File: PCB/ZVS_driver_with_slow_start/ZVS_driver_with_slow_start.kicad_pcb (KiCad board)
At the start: 2 copper layers, 31 parts, among them J1 Battery_12v_Connection, J2 Power_Switch, J3 ON_switch, J4 Conn_01x02_Socket, Q1 IRF640NPbF, Q2 IRF640NPbF, Q3 IRF640NPbF, U1 OP07, U2 OP07

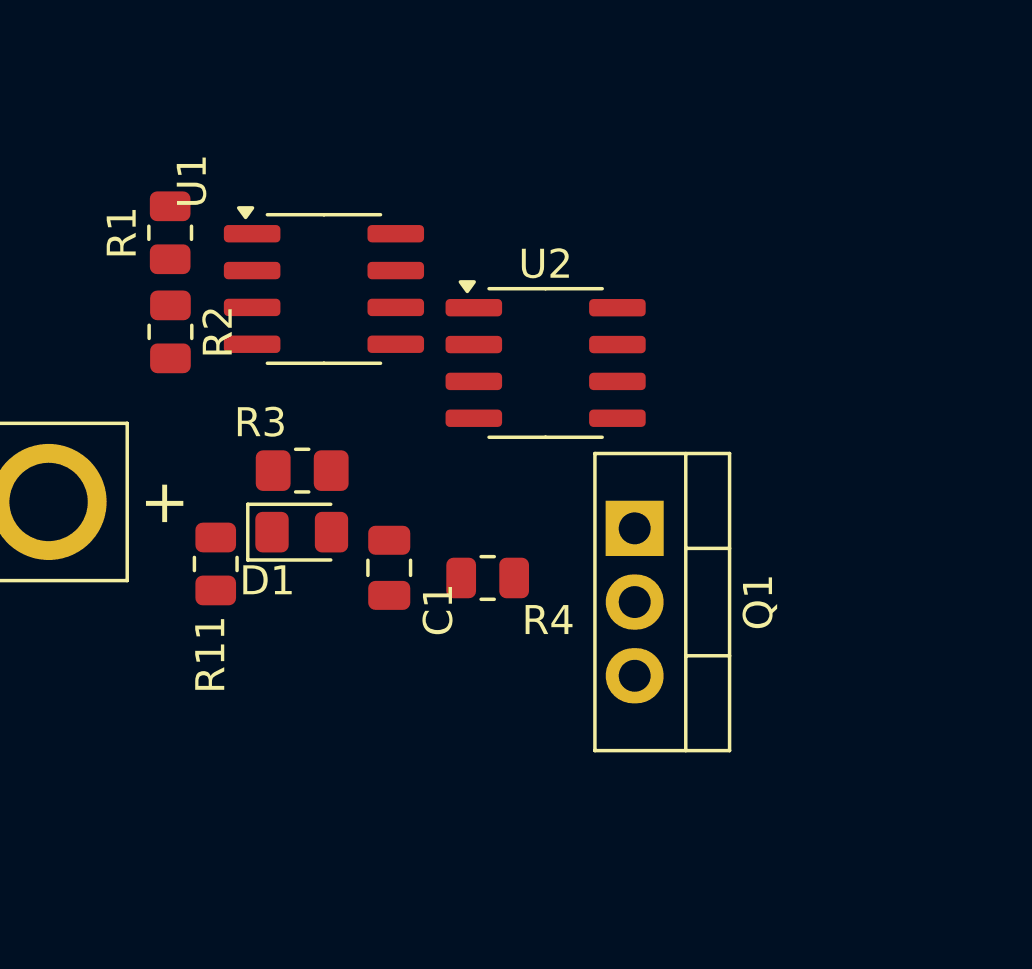
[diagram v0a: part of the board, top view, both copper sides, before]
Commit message: added curent limiting RL on Q1
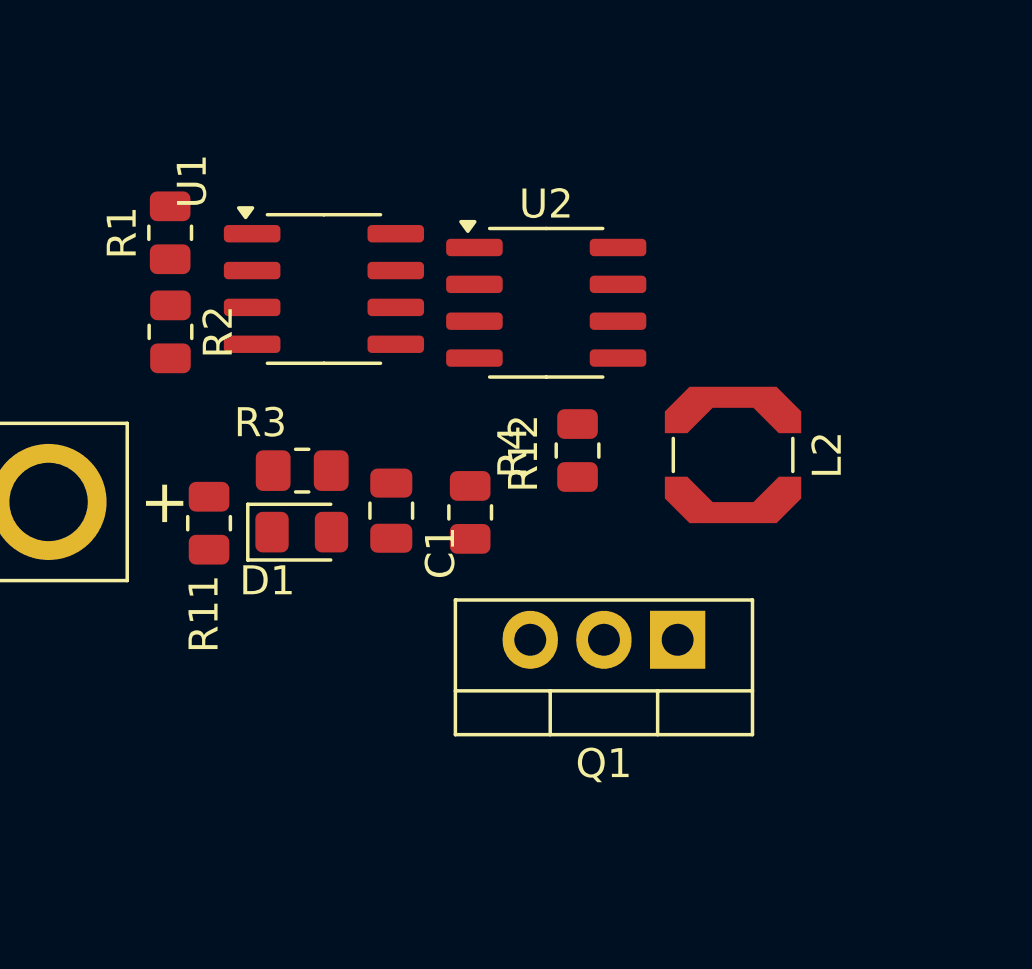
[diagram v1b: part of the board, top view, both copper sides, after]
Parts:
- added L2: 100u, Inductor_SMD:L_Coilcraft_LPS4414, F.Cu at (71.8, 106.5)
- added R12: 100, Resistor_SMD:R_0805_2012Metric, F.Cu at (66.4, 106.4)
- moved Q1 4.12 mm to (69.9, 112.9), turned to 180 degrees
- moved R4 2.34 mm to (62.7, 108.5), turned to -90 degrees
- moved U2 2.08 mm to (65.3, 101.3)
- moved C1 1.97 mm to (60.0, 108.4)
- moved R11 1.42 mm to (53.7, 108.9)
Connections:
- U2 pad 6: Net-(Q1-G) -> Net-(L2-Pad1)

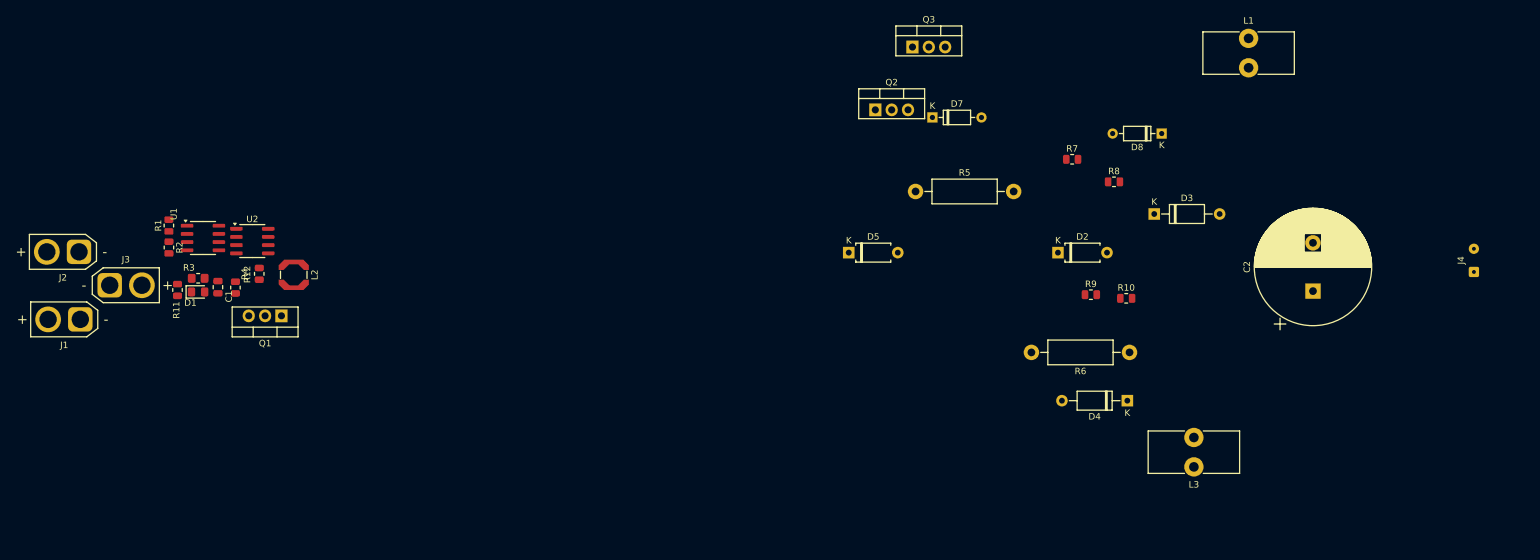
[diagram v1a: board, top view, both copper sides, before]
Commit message: added fuse and cleaned up board
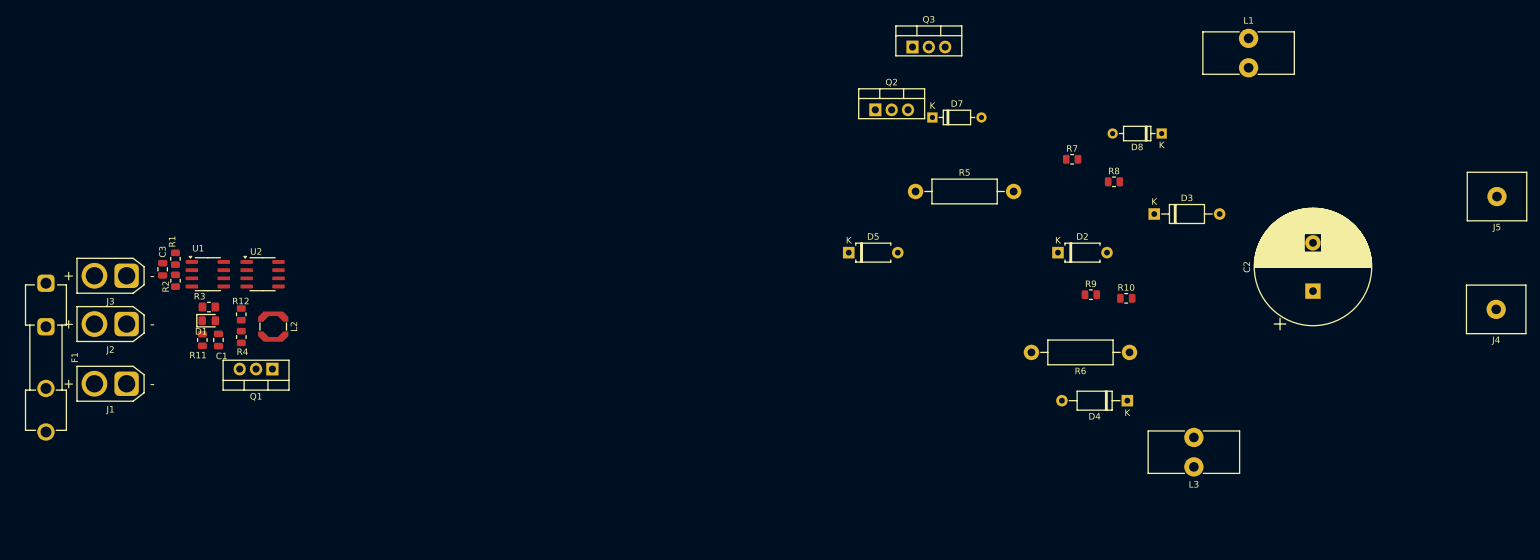
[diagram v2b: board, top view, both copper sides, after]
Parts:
- added C3: 100u, Capacitor_SMD:C_0805_2012Metric, F.Cu at (51.4, 105.7)
- added F1: Fuse, Fuse:Fuseholder_Clip-5x20mm_Keystone_3517_Inline_P23.11x6.76mm_D1.70mm_Horizontal, F.Cu at (33.3, 107.8)
- added J5: Conn_01x01, TerminalBlock_MetzConnect:TerminalBlock_MetzConnect_360271_1x01_Horizontal_ScrewM3.0_Boxed, F.Cu at (258.7, 94.4)
- J4: value Conn_01x02_Socket -> Conn_01x01; footprint Connector_Wire:SolderWire-0.1sqmm_1x02_P3.6mm_D0.4mm_OD1mm -> TerminalBlock_MetzConnect:TerminalBlock_MetzConnect_360271_1x01_Horizontal_ScrewM3.0_Boxed
- moved J2 13.4 mm to (45.8, 114.2)
- moved J1 12.3 mm to (45.8, 123.4)
- moved R11 8.68 mm to (57.6, 116.6)
- moved L2 8.64 mm to (68.6, 114.6)
- moved Q1 8.39 mm to (68.5, 121.2)
- moved C1 8.21 mm to (60.1, 116.6)
- moved R4 7.74 mm to (63.6, 116.2)
- moved R12 6.88 mm to (63.6, 112.7)
- moved J4 6.77 mm to (258.6, 111.9), turned to 180 degrees
- moved U1 5.68 mm to (58.4, 106.4)
- moved U2 5.39 mm to (66.9, 106.4)
- moved R1 5.26 mm to (53.4, 104.0)
- moved R2 5.26 mm to (53.4, 107.4)
- moved D1 4.77 mm to (58.6, 113.6)
- moved R3 4.77 mm to (58.6, 111.5)
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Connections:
- J2 pad 2: Net-(J1-Pin_2) -> Net-(J2-Pin_2)
- J3 pad 1: Net-(D3-K) -> Net-(D1-K)
- J3 pad 2: Net-(D1-K) -> Net-(D3-K)

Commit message: the PCB is taking some serious shape
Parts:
- removed Q2: IRF640NPbF, Package_TO_SOT_THT:TO-220-3_Vertical
- added Q4: IRF640NPbF, Package_TO_SOT_THT:TO-220-3_Vertical, F.Cu at (118.6, 131.4)
- added R13: 100M, Resistor_THT:R_Axial_DIN0411_L9.9mm_D3.6mm_P15.24mm_Horizontal, F.Cu at (85.2, 113.3)
- C2: footprint Capacitor_THT:CP_Radial_D18.0mm_P7.50mm -> Capacitor_THT:C_Rect_L16.5mm_W9.0mm_P15.00mm_MKT
- R10, R7, R8, R9: footprint Resistor_SMD:R_0805_2012Metric -> Resistor_THT:R_Axial_DIN0207_L6.3mm_D2.5mm_P7.62mm_Horizontal
- R5, R6: footprint Resistor_THT:R_Axial_DIN0411_L9.9mm_D3.6mm_P15.24mm_Horizontal -> Resistor_THT:R_Axial_DIN0207_L6.3mm_D2.5mm_P7.62mm_Horizontal
- moved L1 120.0 mm to (107.0, 110.1), turned to 180 degrees
- moved D3 110.2 mm to (96.1, 111.2), turned to 90 degrees
- moved D4 105.5 mm to (96.2, 135.0), turned to -90 degrees
- moved L3 104.2 mm to (107.6, 141.7)
- moved J5 104.2 mm to (160.7, 129.6)
- moved R7 99.3 mm to (103.5, 132.2), turned to 180 degrees
- moved R6 98.2 mm to (107.2, 145.4)
- moved R8 98.1 mm to (103.7, 114.3), turned to 180 degrees
- moved J4 97.7 mm to (160.9, 116.1)
- moved C2 92.7 mm to (137.6, 114.7), turned to -90 degrees
- moved R10 91.8 mm to (110.2, 122.6), turned to 90 degrees
- moved R9 88.5 mm to (110.1, 132.4), turned to 90 degrees
- moved D8 86.9 mm to (123.7, 110.7)
- moved D2 84.4 mm to (107.0, 114.9), turned to -90 degrees
- moved D7 71.3 mm to (123.8, 135.5), turned to 180 degrees
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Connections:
- C3 pad 1: Net-(D3-K) -> /VBUS
- D2 pad 2: Net-(D2-A) -> GND
- D3 pad 1: Net-(D3-K) -> /VBUS
- D4 pad 1: Net-(D3-K) -> /VBUS
- D5 pad 2: Net-(D2-A) -> GND
- F1 pad 1: Net-(J2-Pin_2) -> /VBUS
- F1 pad 2: Net-(J1-Pin_2) -> /VBUS
- J1 pad 2: Net-(J1-Pin_2) -> /VBUS
- J2 pad 1: Net-(D3-K) -> /VBUS
- J2 pad 2: Net-(J2-Pin_2) -> /VBUS
- J3 pad 2: Net-(D3-K) -> /VBUS
- L1 pad 1: Net-(D3-K) -> /VBUS
- L1 pad 2: Net-(D7-K) -> Net-(D8-K)
- L3 pad 1: Net-(D8-K) -> Net-(D7-K)
- L3 pad 2: Net-(D3-K) -> /VBUS
- Q1 pad 2: Net-(D2-A) -> GND
- Q3 pad 2: Net-(D2-A) -> Net-(D7-K)
- Q3 pad 3: Net-(D7-K) -> GND
- R1 pad 2: Net-(D3-K) -> /VBUS
- R10 pad 1: Net-(D2-A) -> GND
- R5 pad 1: Net-(D7-K) -> Net-(D8-K)
- R6 pad 1: Net-(D8-K) -> Net-(D7-K)
- R7 pad 2: Net-(D3-K) -> /VBUS
- R8 pad 2: Net-(D3-K) -> /VBUS
- R9 pad 2: Net-(D2-A) -> GND
- U1 pad 7: Net-(D3-K) -> /VBUS
- U2 pad 7: Net-(D3-K) -> /VBUS

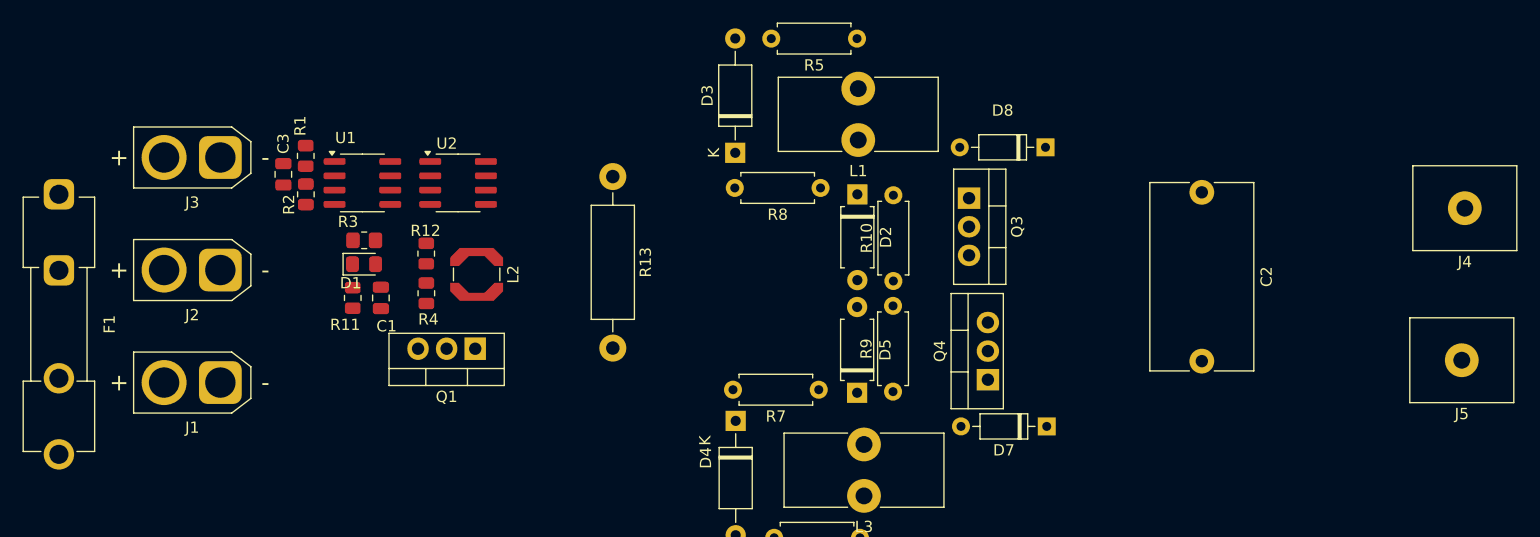
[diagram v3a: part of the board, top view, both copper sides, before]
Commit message: removed superflous power switch
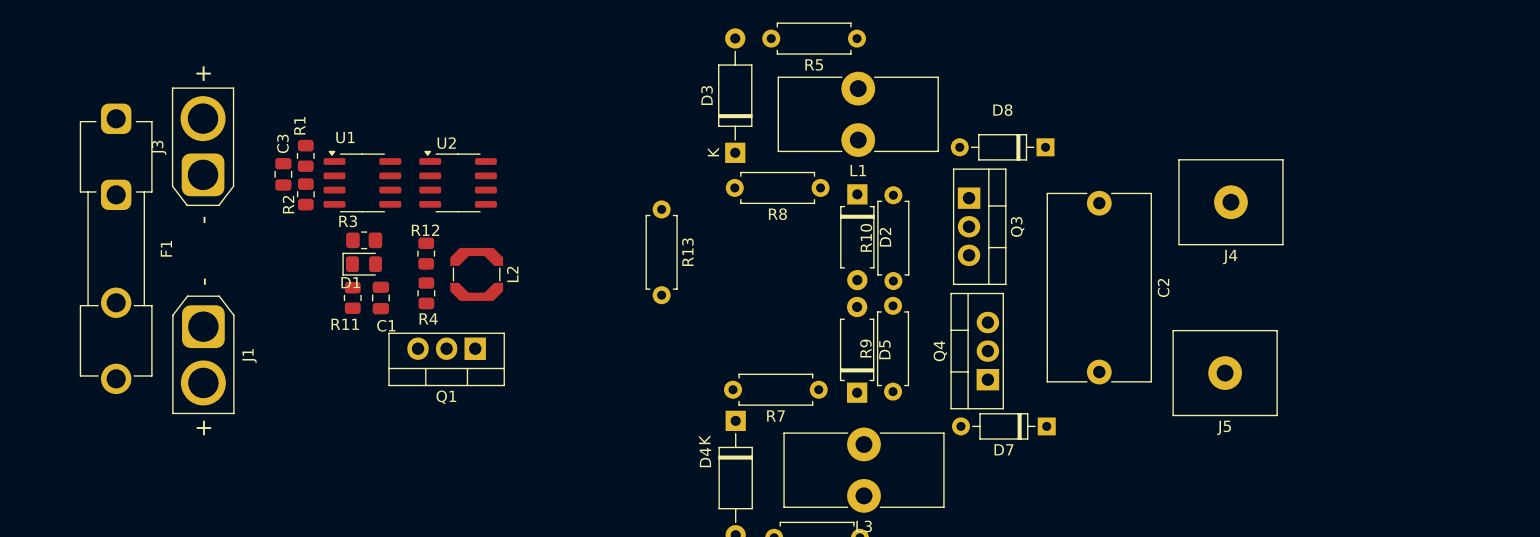
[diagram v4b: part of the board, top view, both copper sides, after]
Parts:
- removed J2: Power_Switch, Connector_AMASS:AMASS_XT30U-F_1x02_P5.0mm_Vertical
- R13: footprint Resistor_THT:R_Axial_DIN0411_L9.9mm_D3.6mm_P15.24mm_Horizontal -> Resistor_THT:R_Axial_DIN0207_L6.3mm_D2.5mm_P7.62mm_Horizontal
- moved J5 21.1 mm to (139.7, 130.8)
- moved J4 20.8 mm to (140.2, 115.6)
- moved C2 9.16 mm to (128.5, 115.7)
- moved F1 8.42 mm to (41.1, 108.2)
- moved R13 5.23 mm to (89.6, 116.2)
- moved J1 5.19 mm to (48.9, 126.7), turned to -90 degrees
- moved J3 2.18 mm to (48.8, 113.2), turned to 90 degrees
